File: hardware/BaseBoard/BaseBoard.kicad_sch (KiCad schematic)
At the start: 109 parts, among them IC1 PCF8574RGTR, J1-ESP1 ESP-1-L, J1-ESP2 ESP-1-L, J1-ESP3 ESP-1-L, J1-ESP4 ESP-1-L, J1-ESP5 ESP-1-L, J1-ESP6 ESP-1-L, J1-ESP7 ESP-1-L, J1-ESP8 ESP-1-L, J2-ESP1 ESP-1-R, J2-ESP2 ESP-1-R, J2-ESP3 ESP-1-R, J2-ESP4 ESP-1-R, J2-ESP5 ESP-1-R, J2-ESP6 ESP-1-R, J2-ESP7 ESP-1-R, J2-ESP8 ESP-1-R, J3-BUS1 BUS-IN, J3-BUS2 BUS-IN, J3-BUS3 BUS-IN, J3-BUS4 BUS-IN, J3-BUS5 BUS-IN, J3-BUS6 BUS-IN, J3-BUS7 BUS-IN, J3-BUS8 BUS-IN, J4-BUS1 BUS-OUT, J4-BUS2 BUS-OUT, J4-BUS3 BUS-OUT, J4-BUS4 BUS-OUT, J4-BUS5 BUS-OUT, J4-BUS6 BUS-OUT, J4-BUS7 BUS-OUT, J4-BUS8 BUS-OUT, Q1 AO3401A, Q2 AO3401A, Q3 AO3401A, Q4 AO3401A, Q5 AO3401A, Q6 AO3401A, Q7 AO3401A, Q8 AO3401A, SW1 SW_DIP_SPSTx03

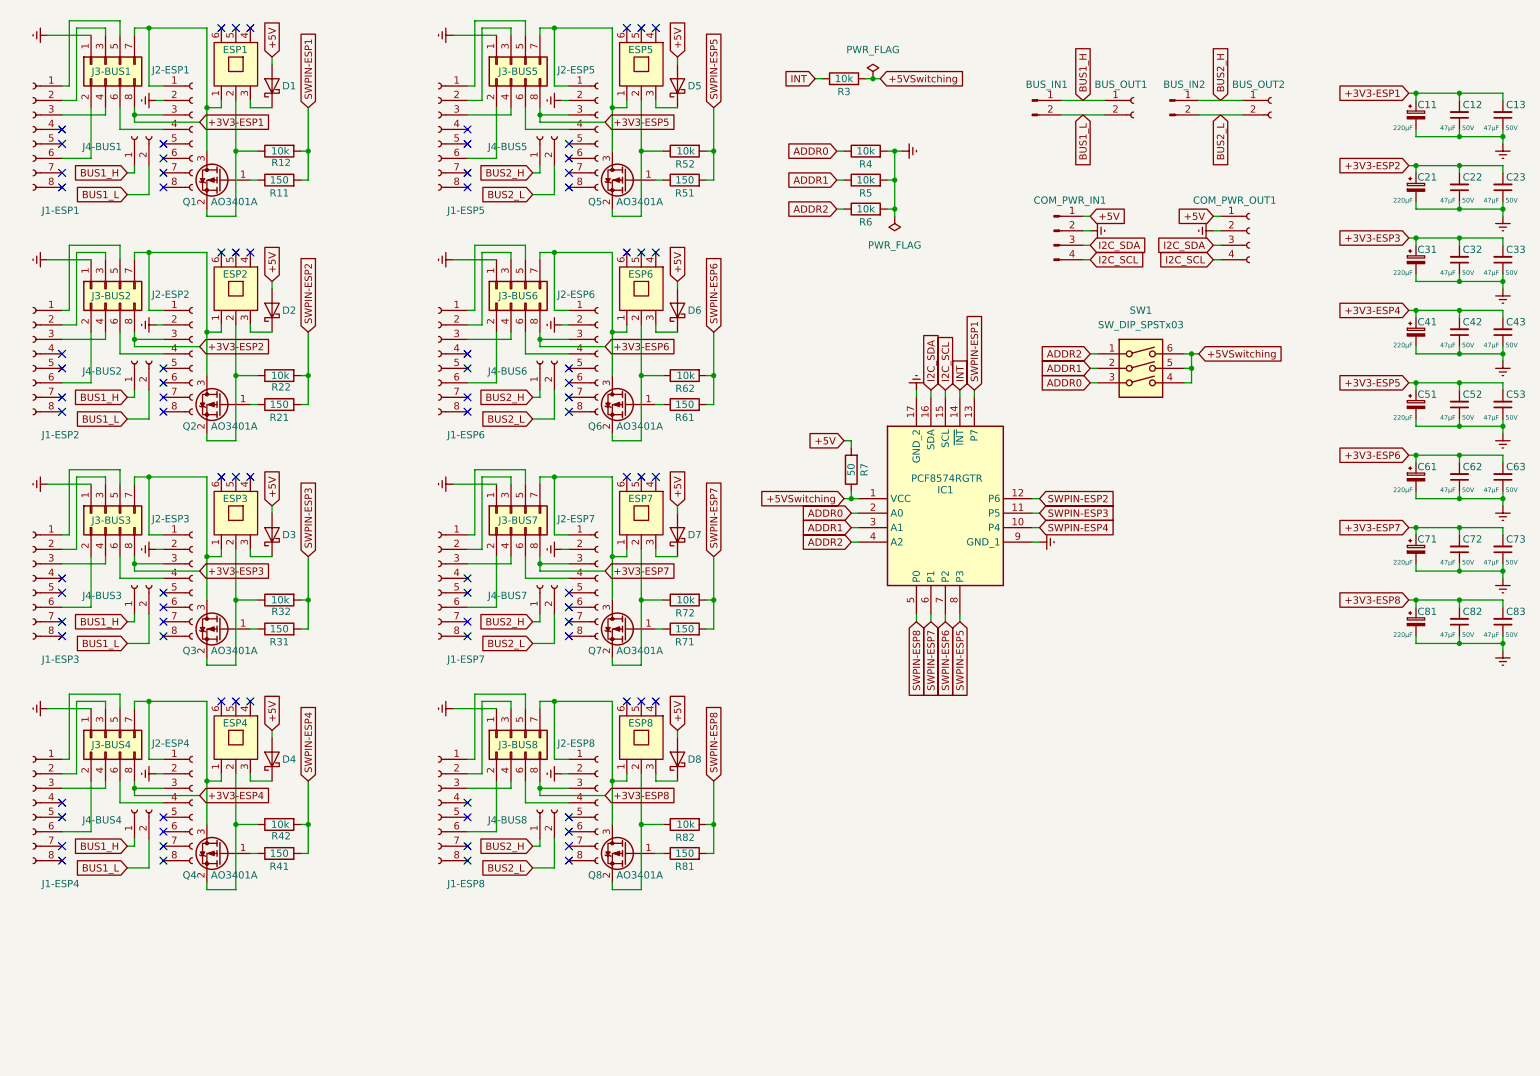
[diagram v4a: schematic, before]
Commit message: Updated BaseBoard to kicad v10.
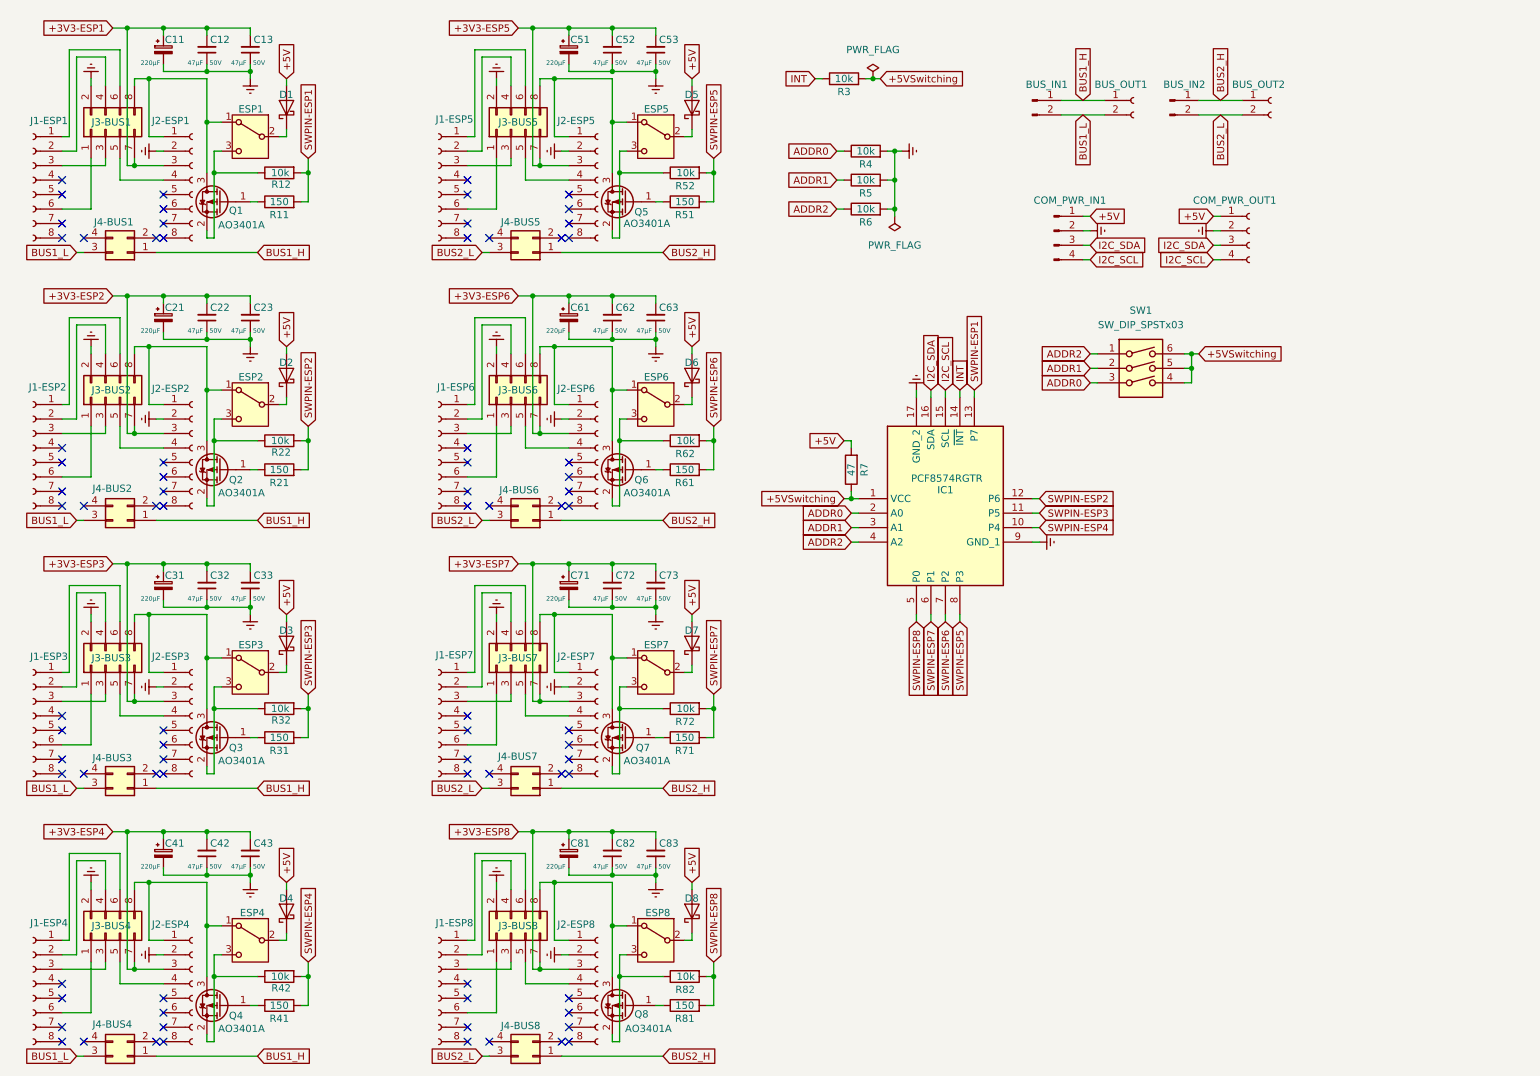
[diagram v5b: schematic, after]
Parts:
- C11, C21, C31, C41, C51, C61, C71, C81: footprint Capacitor_SMD:CP_Elec_6.3x7.7 -> Capacitor_THT:CP_Radial_D6.3mm_P2.50mm
- ESP1, ESP2, ESP3, ESP4, ESP5, ESP6, ESP7, ESP8: footprint sw_dpdt_xlx:SW_DPDT_XLX -> LIB_CL-SB-12B-01T:CLSB12B01T; symbol sw_dpdt_xlx:SW_DPDT_XLX -> Switch:SW_SPDT; now in the parts list
- J3-BUS1, J3-BUS2, J3-BUS3, J3-BUS4, J3-BUS5, J3-BUS6, J3-BUS7, J3-BUS8: footprint Connector_PinSocket_2.54mm:PinSocket_2x04_P2.54mm_Vertical -> Connector_Wuerth:Wuerth_WR-PHD_61300825721_Standard_2x04_P2.54mm_Vertical
- J4-BUS1, J4-BUS2, J4-BUS3, J4-BUS4, J4-BUS5, J4-BUS6, J4-BUS7, J4-BUS8: footprint Connector_PinSocket_2.54mm:PinSocket_1x02_P2.54mm_Vertical -> Connector_Wuerth:Wuerth_WR-PHD_61300425721_Standard_2x02_P2.54mm_Vertical; symbol Connector:Conn_01x02_Socket -> Connector_Generic:Conn_02x02_Top_Bottom; now in the parts list
- R7: value 50 -> 47
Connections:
- net +3V3-ESP1: now also J3-BUS1.7 (Pin_7); no longer J3-BUS1.8 (Pin_8)
- net +3V3-ESP2: now also J3-BUS2.7 (Pin_7); no longer J3-BUS2.8 (Pin_8)
- net +3V3-ESP3: now also J3-BUS3.7 (Pin_7); no longer J3-BUS3.8 (Pin_8)
- net +3V3-ESP4: now also J3-BUS4.7 (Pin_7); no longer J3-BUS4.8 (Pin_8)
- net +3V3-ESP5: now also J3-BUS5.7 (Pin_7); no longer J3-BUS5.8 (Pin_8)
- net +3V3-ESP6: now also J3-BUS6.7 (Pin_7); no longer J3-BUS6.8 (Pin_8)
- net +3V3-ESP7: now also J3-BUS7.7 (Pin_7); no longer J3-BUS7.8 (Pin_8)
- net +3V3-ESP8: now also J3-BUS8.7 (Pin_7); no longer J3-BUS8.8 (Pin_8)
- net BUS1_L: now also J4-BUS1.3 (Pin_3), J4-BUS2.3 (Pin_3), J4-BUS3.3 (Pin_3), J4-BUS4.3 (Pin_3); no longer J4-BUS1.2 (Pin_2), J4-BUS2.2 (Pin_2), J4-BUS3.2 (Pin_2), J4-BUS4.2 (Pin_2)
- net BUS2_L: now also J4-BUS5.3 (Pin_3), J4-BUS6.3 (Pin_3), J4-BUS7.3 (Pin_3), J4-BUS8.3 (Pin_3); no longer J4-BUS5.2 (Pin_2), J4-BUS6.2 (Pin_2), J4-BUS7.2 (Pin_2), J4-BUS8.2 (Pin_2)
- net GNDREF: now also J3-BUS1.2 (Pin_2), J3-BUS2.2 (Pin_2), J3-BUS3.2 (Pin_2), J3-BUS4.2 (Pin_2), J3-BUS5.2 (Pin_2), J3-BUS6.2 (Pin_2), J3-BUS7.2 (Pin_2), J3-BUS8.2 (Pin_2); no longer J3-BUS1.1 (Pin_1), J3-BUS2.1 (Pin_1), J3-BUS3.1 (Pin_1), J3-BUS4.1 (Pin_1), J3-BUS5.1 (Pin_1), J3-BUS6.1 (Pin_1), J3-BUS7.1 (Pin_1), J3-BUS8.1 (Pin_1)
- net at Q2.2 (S), R22.1: now also ESP2.3 (C); no longer ESP2.2
- net at J1-ESP7.6 (Pin_6): now also J3-BUS7.1 (Pin_1); no longer J3-BUS7.2 (Pin_2)
- net at J3-BUS7.3 (Pin_3): now also J1-ESP7.3 (Pin_3); no longer J1-ESP7.2 (Pin_2)
- net at J3-BUS7.4 (Pin_4): now also J1-ESP7.2 (Pin_2); no longer J1-ESP7.3 (Pin_3)
- net at J3-BUS7.5 (Pin_5): now also J2-ESP7.4 (Pin_4); no longer J1-ESP7.1 (Pin_1)
- net at J3-BUS7.6 (Pin_6): now also J1-ESP7.1 (Pin_1); no longer J2-ESP7.4 (Pin_4)
- net at ESP7.1 (A), J2-ESP7.1 (Pin_1), Q7.3 (D): now also J3-BUS7.8 (Pin_8); no longer J3-BUS7.7 (Pin_7)
- net at ESP4.1 (A), J2-ESP4.1 (Pin_1), Q4.3 (D): now also J3-BUS4.8 (Pin_8); no longer J3-BUS4.7 (Pin_7)
- net at J2-ESP4.4 (Pin_4): now also J3-BUS4.5 (Pin_5); no longer J3-BUS4.6 (Pin_6)
- net at D6.1 (K): now also ESP6.2 (B); no longer ESP6.3
- net at J1-ESP2.6 (Pin_6): now also J3-BUS2.1 (Pin_1); no longer J3-BUS2.2 (Pin_2)
- net at J3-BUS2.3 (Pin_3): now also J1-ESP2.3 (Pin_3); no longer J1-ESP2.2 (Pin_2)
- net at J3-BUS2.4 (Pin_4): now also J1-ESP2.2 (Pin_2); no longer J1-ESP2.3 (Pin_3)
- net at J3-BUS2.5 (Pin_5): now also J2-ESP2.4 (Pin_4); no longer J1-ESP2.1 (Pin_1)
- net at J3-BUS2.6 (Pin_6): now also J1-ESP2.1 (Pin_1); no longer J2-ESP2.4 (Pin_4)
- net at ESP2.1 (A), J2-ESP2.1 (Pin_1), Q2.3 (D): now also J3-BUS2.8 (Pin_8); no longer J3-BUS2.7 (Pin_7)
- net at ESP8.1 (A), J2-ESP8.1 (Pin_1), Q8.3 (D): now also J3-BUS8.8 (Pin_8); no longer J3-BUS8.7 (Pin_7)
- net at J2-ESP8.4 (Pin_4): now also J3-BUS8.5 (Pin_5); no longer J3-BUS8.6 (Pin_6)
- net at D1.1 (K): now also ESP1.2 (B); no longer ESP1.3
- net at Q6.2 (S), R62.1: now also ESP6.3 (C); no longer ESP6.2
- net at ESP6.1 (A), J2-ESP6.1 (Pin_1), Q6.3 (D): now also J3-BUS6.8 (Pin_8); no longer J3-BUS6.7 (Pin_7)
- net at J1-ESP1.6 (Pin_6): now also J3-BUS1.1 (Pin_1); no longer J3-BUS1.2 (Pin_2)
- net at J3-BUS1.3 (Pin_3): now also J1-ESP1.3 (Pin_3); no longer J1-ESP1.2 (Pin_2)
- net at J3-BUS1.4 (Pin_4): now also J1-ESP1.2 (Pin_2); no longer J1-ESP1.3 (Pin_3)
- net at J3-BUS1.5 (Pin_5): now also J2-ESP1.4 (Pin_4); no longer J1-ESP1.1 (Pin_1)
- net at J3-BUS1.6 (Pin_6): now also J1-ESP1.1 (Pin_1); no longer J2-ESP1.4 (Pin_4)
- net at ESP1.1 (A), J2-ESP1.1 (Pin_1), Q1.3 (D): now also J3-BUS1.8 (Pin_8); no longer J3-BUS1.7 (Pin_7)
- net at Q5.2 (S), R52.1: now also ESP5.3 (C); no longer ESP5.2
- net at ESP5.1 (A), J2-ESP5.1 (Pin_1), Q5.3 (D): now also J3-BUS5.8 (Pin_8); no longer J3-BUS5.7 (Pin_7)
- net at Q8.2 (S), R82.1: now also ESP8.3 (C); no longer ESP8.2
- net at D8.1 (K): now also ESP8.2 (B); no longer ESP8.3
- net at Q7.2 (S), R72.1: now also ESP7.3 (C); no longer ESP7.2
- net at Q1.2 (S), R12.1: now also ESP1.3 (C); no longer ESP1.2
- net at D5.1 (K): now also ESP5.2 (B); no longer ESP5.3
- net at J1-ESP8.6 (Pin_6): now also J3-BUS8.1 (Pin_1); no longer J3-BUS8.2 (Pin_2)
- net at J3-BUS8.3 (Pin_3): now also J1-ESP8.3 (Pin_3); no longer J1-ESP8.2 (Pin_2)
- net at J3-BUS8.4 (Pin_4): now also J1-ESP8.2 (Pin_2); no longer J1-ESP8.3 (Pin_3)
- net at J1-ESP8.1 (Pin_1): now also J3-BUS8.6 (Pin_6); no longer J3-BUS8.5 (Pin_5)
- net at D7.1 (K): now also ESP7.2 (B); no longer ESP7.3
- net at Q4.2 (S), R42.1: now also ESP4.3 (C); no longer ESP4.2
- net at Q3.2 (S), R32.1: now also ESP3.3 (C); no longer ESP3.2
- net at ESP3.1 (A), J2-ESP3.1 (Pin_1), Q3.3 (D): now also J3-BUS3.8 (Pin_8); no longer J3-BUS3.7 (Pin_7)
- net at D4.1 (K): now also ESP4.2 (B); no longer ESP4.3
- net at J1-ESP3.6 (Pin_6): now also J3-BUS3.1 (Pin_1); no longer J3-BUS3.2 (Pin_2)
- net at J3-BUS3.3 (Pin_3): now also J1-ESP3.3 (Pin_3); no longer J1-ESP3.2 (Pin_2)
- net at J3-BUS3.4 (Pin_4): now also J1-ESP3.2 (Pin_2); no longer J1-ESP3.3 (Pin_3)
- net at J3-BUS3.5 (Pin_5): now also J2-ESP3.4 (Pin_4); no longer J1-ESP3.1 (Pin_1)
- net at J3-BUS3.6 (Pin_6): now also J1-ESP3.1 (Pin_1); no longer J2-ESP3.4 (Pin_4)
- net at J1-ESP4.1 (Pin_1): now also J3-BUS4.6 (Pin_6); no longer J3-BUS4.5 (Pin_5)
- net at J1-ESP4.2 (Pin_2): now also J3-BUS4.4 (Pin_4); no longer J3-BUS4.3 (Pin_3)
- net at J1-ESP4.3 (Pin_3): now also J3-BUS4.3 (Pin_3); no longer J3-BUS4.4 (Pin_4)
- net at J1-ESP4.6 (Pin_6): now also J3-BUS4.1 (Pin_1); no longer J3-BUS4.2 (Pin_2)
- net at D3.1 (K): now also ESP3.2 (B); no longer ESP3.3
- net at D2.1 (K): now also ESP2.2 (B); no longer ESP2.3
- net at J1-ESP6.6 (Pin_6): now also J3-BUS6.1 (Pin_1); no longer J3-BUS6.2 (Pin_2)
- net at J3-BUS6.3 (Pin_3): now also J1-ESP6.3 (Pin_3); no longer J1-ESP6.2 (Pin_2)
- net at J3-BUS6.4 (Pin_4): now also J1-ESP6.2 (Pin_2); no longer J1-ESP6.3 (Pin_3)
- net at J3-BUS6.5 (Pin_5): now also J2-ESP6.4 (Pin_4); no longer J1-ESP6.1 (Pin_1)
- net at J3-BUS6.6 (Pin_6): now also J1-ESP6.1 (Pin_1); no longer J2-ESP6.4 (Pin_4)
- net at J1-ESP5.6 (Pin_6): now also J3-BUS5.1 (Pin_1); no longer J3-BUS5.2 (Pin_2)
- net at J3-BUS5.3 (Pin_3): now also J1-ESP5.3 (Pin_3); no longer J1-ESP5.2 (Pin_2)
- net at J3-BUS5.4 (Pin_4): now also J1-ESP5.2 (Pin_2); no longer J1-ESP5.3 (Pin_3)
- net at J3-BUS5.5 (Pin_5): now also J2-ESP5.4 (Pin_4); no longer J1-ESP5.1 (Pin_1)
- net at J3-BUS5.6 (Pin_6): now also J1-ESP5.1 (Pin_1); no longer J2-ESP5.4 (Pin_4)
- no-connect marks 88 -> 80
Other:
- moved on the sheet: C11, C12, C13, C21, C22, C23, C31, C32, C33, C41, C42, C43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

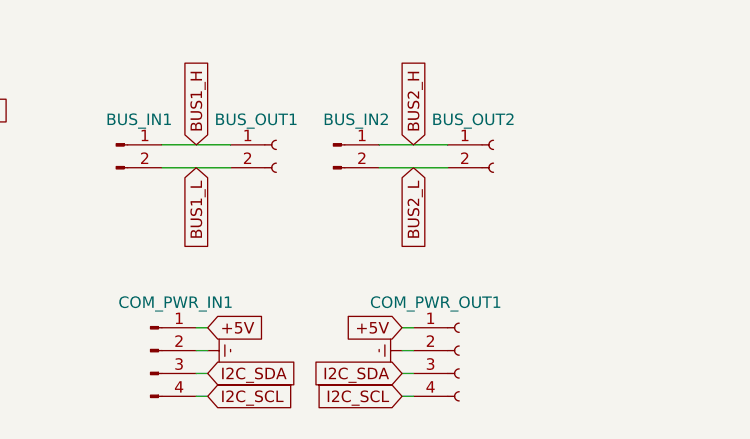
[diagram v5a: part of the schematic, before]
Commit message: Minor imrpovements in positions and footprints.
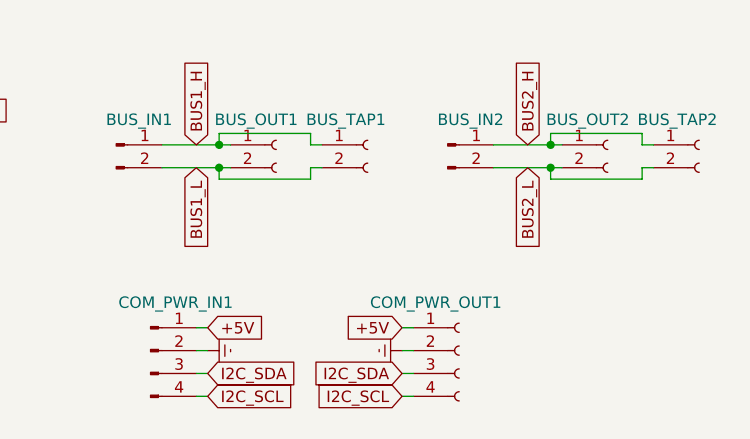
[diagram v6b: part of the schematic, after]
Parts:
- added BUS_TAP1, BUS_TAP2: Conn_01x02_Socket, Connector_PinHeader_2.54mm:PinHeader_1x02_P2.54mm_Vertical, symbol Connector:Conn_01x02_Socket
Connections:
- net BUS1_H: now also BUS_TAP1.1 (Pin_1)
- net BUS1_L: now also BUS_TAP1.2 (Pin_2)
- net BUS2_H: now also BUS_TAP2.1 (Pin_1)
- net BUS2_L: now also BUS_TAP2.2 (Pin_2)
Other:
- moved on the sheet: BUS_IN2, BUS_OUT2
